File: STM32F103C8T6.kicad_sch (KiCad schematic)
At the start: 32 parts, among them J1 USB_B_Micro, J2 Conn_01x04_Pin, J3 Conn_01x04_Pin, J4 Conn_01x04_Pin, SW1 SW_SPDT, U1 STM32F103C8T6, U2 AMS1117-3.3, Y1 16MHz

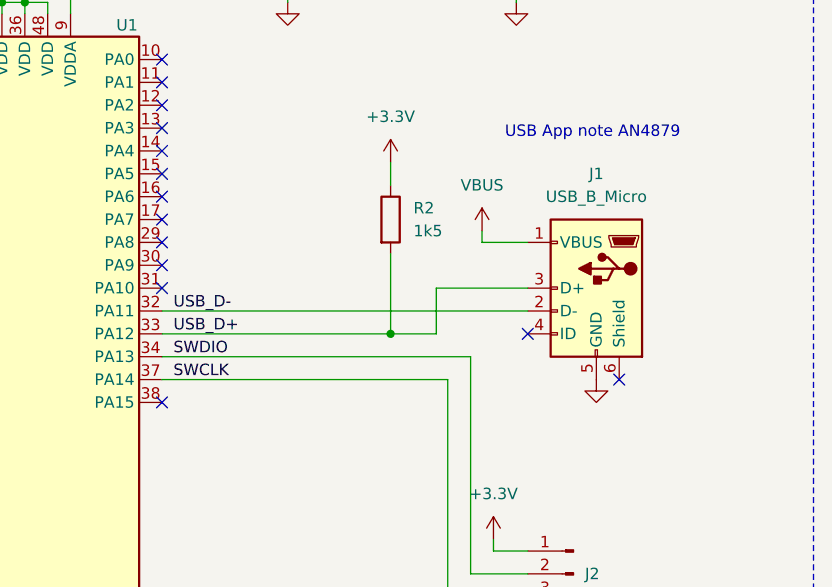
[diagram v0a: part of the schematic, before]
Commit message: updated footprints to ones which have stocks at JLCPCB
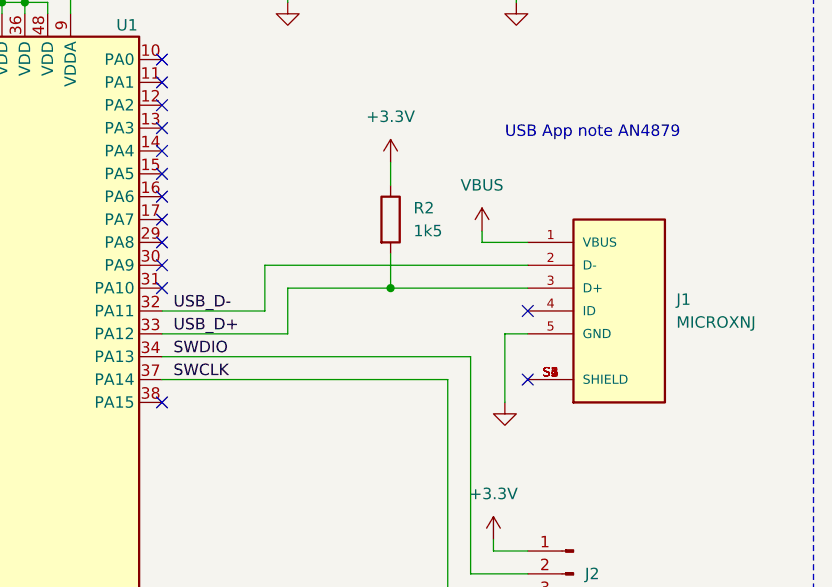
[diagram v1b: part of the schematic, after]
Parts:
- removed J1: USB_B_Micro, Connector_USB:USB_Micro-B_Wuerth_629105150521, symbol Connector:USB_B_Micro
- added J1: MICROXNJ, project_footprints:SHOUHAN_MICROXNJ, symbol MICROXNJ:MICROXNJ
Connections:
- net GND: now also J1.5 (GND)
- net USB_D+: now also J1.3 (D+)
- net USB_D-: now also J1.2 (D-)
- net VBUS: now also J1.1 (VBUS)
- new net: J1.S1 (SHIELD), J1.S2 (SHIELD), J1.S3 (SHIELD), J1.S4 (SHIELD), J1.S5 (SHIELD), J1.S6 (SHIELD)
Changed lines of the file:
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@@
   (junction (at 189.23 39.37) (diameter 0) (color 0 0 0 0)
   )
-  (junction (at 224.79 86.36) (diameter 0) (color 0 0 0 0)
-  )
   (junction (at 24.13 38.1) (diameter 0) (color 0 0 0 0)
   )
@@
   )
   (junction (at 120.65 46.99) (diameter 0) (color 0 0 0 0)
+  )
+  (junction (at 224.79 81.28) (diameter 0) (color 0 0 0 0)
   )
   (junction (at 116.84 104.14) (diameter 0) (color 0 0 0 0)
@@
   (no_connect (at 166.37 104.14))
   (no_connect (at 199.39 81.28))
+  (no_connect (at 240.03 91.44))
   (no_connect (at 166.37 114.3))
   (no_connect (at 166.37 119.38))
   (no_connect (at 199.39 60.96))
+  (no_connect (at 240.03 83.82))
   (no_connect (at 166.37 91.44))
-  (no_connect (at 240.03 86.36))
   (no_connect (at 199.39 55.88))
   (no_connect (at 199.39 68.58))
-  (no_connect (at 250.19 91.44))
   (no_connect (at 166.37 93.98))
   (no_connect (at 166.37 121.92))
@@
     (stroke (width 0) (type default))
   )
+  (wire (pts (xy 213.36 81.28) (xy 224.79 81.28))
+    (stroke (width 0) (type default))
+  )
   (wire (pts (xy 109.22 76.2) (xy 109.22 85.09))
     (stroke (width 0) (type default))
@@
     (stroke (width 0) (type default))
   )
-  (wire (pts (xy 240.03 81.28) (xy 229.87 81.28))
+  (wire (pts (xy 224.79 81.28) (xy 240.03 81.28))
     (stroke (width 0) (type default))
   )
@@
     (stroke (width 0) (type default))
   )
-  (wire (pts (xy 229.87 86.36) (xy 224.79 86.36))
+  (wire (pts (xy 237.49 86.36) (xy 240.03 86.36))
     (stroke (width 0) (type default))
   )
@@
   )
   (wire (pts (xy 116.84 104.14) (xy 109.22 104.14))
+    (stroke (width 0) (type default))
+  )
+  (wire (pts (xy 237.49 93.98) (xy 237.49 86.36))
     (stroke (width 0) (type default))
   )
@@
     (stroke (width 0) (type default))
   )
-  (wire (pts (xy 224.79 86.36) (xy 199.39 86.36))
-    (stroke (width 0) (type default))
-  )
   (wire (pts (xy 129.54 147.32) (xy 130.81 147.32))
     (stroke (width 0) (type default))
@@
     (stroke (width 0) (type default))
   )
+  (wire (pts (xy 199.39 86.36) (xy 213.36 86.36))
+    (stroke (width 0) (type default))
+  )
   (wire (pts (xy 143.51 39.37) (xy 154.94 39.37))
     (stroke (width 0) (type default))
@@
     (stroke (width 0) (type default))
   )
-  (wire (pts (xy 229.87 81.28) (xy 229.87 86.36))
+  (wire (pts (xy 213.36 86.36) (xy 213.36 81.28))
     (stroke (width 0) (type default))
   )
@@
     (stroke (width 0) (type default))
   )
-  (wire (pts (xy 224.79 77.47) (xy 224.79 86.36))
+  (wire (pts (xy 224.79 77.47) (xy 224.79 81.28))
     (stroke (width 0) (type default))
   )
@@
     (stroke (width 0) (type default))
   )
+  (wire (pts (xy 210.82 78.74) (xy 240.03 78.74))
+    (stroke (width 0) (type default))
+  )
   (wire (pts (xy 154.94 85.09) (xy 154.94 68.58))
     (stroke (width 0) (type default))
@@
     (stroke (width 0) (type default))
   )
-  (wire (pts (xy 199.39 83.82) (xy 240.03 83.82))
+  (wire (pts (xy 199.39 83.82) (xy 210.82 83.82))
     (stroke (width 0) (type default))
   )
@@
   )
   (wire (pts (xy 189.23 39.37) (xy 196.85 39.37))
+    (stroke (width 0) (type default))
+  )
+  (wire (pts (xy 210.82 83.82) (xy 210.82 78.74))
     (stroke (width 0) (type default))
   )
@@
     )
   )
-  (symbol (lib_id "power:GND") (at 247.65 91.44 0) (unit 1)
-    (in_bom yes) (on_board yes) (dnp no) (fields_autoplaced)
-    (property "Reference" "#PWR012" (at 247.65 97.79 0)
-      (effects (font (size 1.27 1.27)) hide)
-    )
-    (property "Value" "GND" (at 247.65 96.52 0)
-      (effects (font (size 1.27 1.27)) hide)
-    )
-    (property "Footprint" "" (at 247.65 91.44 0)
-      (effects (font (size 1.27 1.27)) hide)
-    )
-    (property "Datasheet" "" (at 247.65 91.44 0)
-      (effects (font (size 1.27 1.27)) hide)
-    )
-    (pin "1")
-    (instances
-      (project "STM32F103C8T6"
-        (path "/7affc536-b27a-42a4-bb95-95dd3805b677"
-          (reference "#PWR012") (unit 1)
-        )
-      )
-    )
-  )
   (symbol (lib_id "power:GND") (at 120.65 49.53 0) (unit 1)
     (in_bom yes) (on_board yes) (dnp no) (fields_autoplaced)
@@
     )
   )
+  (symbol (lib_id "power:GND") (at 237.49 93.98 0) (unit 1)
+    (in_bom yes) (on_board yes) (dnp no) (fields_autoplaced)
+    (property "Reference" "#PWR025" (at 237.49 100.33 0)
+      (effects (font (size 1.27 1.27)) hide)
+    )
+    (property "Value" "GND" (at 237.49 99.06 0)
+      (effects (font (size 1.27 1.27)) hide)
+    )
+    (property "Footprint" "" (at 237.49 93.98 0)
+      (effects (font (size 1.27 1.27)) hide)
+    )
+    (property "Datasheet" "" (at 237.49 93.98 0)
+      (effects (font (size 1.27 1.27)) hide)
+    )
+    (pin "1")
+    (instances
+      (project "STM32F103C8T6"
+        (path "/7affc536-b27a-42a4-bb95-95dd3805b677"
+          (reference "#PWR025") (unit 1)
+        )
+      )
+    )
+  )
   (symbol (lib_id "power:GND") (at 24.13 54.61 0) (unit 1)
     (in_bom yes) (on_board yes) (dnp no) (fields_autoplaced)
@@
         (path "/7affc536-b27a-42a4-bb95-95dd3805b677"
           (reference "C8") (unit 1)
-        )
-      )
-    )
-  )
-  (symbol (lib_id "Connector:USB_B_Micro") (at 247.65 81.28 0) (mirror y) (unit 1)
-    (in_bom yes) (on_board yes) (dnp no)
-    (property "Reference" "J1" (at 247.65 68.58 0)
-      (effects (font (size 1.27 1.27)))
-    )
-    (property "Value" "USB_B_Micro" (at 247.65 71.12 0)
-      (effects (font (size 1.27 1.27)))
-    )
-    (property "Footprint" "Connector_USB:USB_Micro-B_Wuerth_629105150521" (at 243.84 82.55 0)
-      (effects (font (size 1.27 1.27)) hide)
-    )
-    (property "Datasheet" "~" (at 243.84 82.55 0)
-      (effects (font (size 1.27 1.27)) hide)
-    )
-    (pin "1")
-    (pin "2")
-    (pin "3")
-    (pin "5")
-    (pin "4")
-    (pin "6")
-    (instances
-      (project "STM32F103C8T6"
-        (path "/7affc536-b27a-42a4-bb95-95dd3805b677"
-          (reference "J1") (unit 1)
         )
       )
@@
         )
       )
+    )
+  )
+  (symbol (lib_id "MICROXNJ:MICROXNJ") (at 250.19 83.82 0) (unit 1)
+    (in_bom yes) (on_board yes) (dnp no) (fields_autoplaced)
+    (property "Reference" "J1" (at 256.54 82.55 0)
+      (effects (font (size 1.27 1.27)) (justify left))
+    )
+    (property "Value" "MICROXNJ" (at 256.54 85.09 0)
+      (effects (font (size 1.27 1.27)) (justify left))
+    )
+    (property "Footprint" "project_footprints:SHOUHAN_MICROXNJ" (at 250.19 83.82 0)
+      (effects (font (size 1.27 1.27)) (justify bottom) hide)
+    )
+    (property "Datasheet" "" (at 250.19 83.82 0)
+      (effects (font (size 1.27 1.27)) hide)
+    )
+    (property "MF" "Shouhan" (at 250.19 83.82 0)
+      (effects (font (size 1.27 1.27)) (justify bottom) hide)
+    )
+    (property "MAXIMUM_PACKAGE_HEIGHT" "3mm" (at 250.19 83.82 0)
+      (effects (font (size 1.27 1.27)) (justify bottom) hide)
+    )
+    (property "Package" "Package" (at 250.19 83.82 0)
+      (effects (font (size 1.27 1.27)) (justify bottom) hide)
+    )
+    (property "Price" "None" (at 250.19 83.82 0)
+      (effects (font (size 1.27 1.27)) (justify bottom) hide)
+    )
+    (property "Check_prices" "https://www.snapeda.com/parts/MICROXNJ/Shouhan/view-part/?ref=eda" (at 250.19 83.82 0)
+      (effects (font (size 1.27 1.27)) (justify bottom) hide)
+    )
+    (property "STANDARD" "Manufacturer Recommendations" (at 250.19 83.82 0)
+      (effects (font (size 1.27 1.27)) (justify bottom) hide)
+    )
+    (property "PARTREV" "A" (at 250.19 83.82 0)
+      (effects (font (size 1.27 1.27)) (justify bottom) hide)
+    )
+    (property "SnapEDA_Link" "https://www.snapeda.com/parts/MICROXNJ/Shouhan/view-part/?ref=snap" (at 250.19 83.82 0)
+      (effects (font (size 1.27 1.27)) (justify bottom) hide)
+    )
+    (property "MP" "MICROXNJ" (at 250.19 83.82 0)
+      (effects (font (size 1.27 1.27)) (justify bottom) hide)
+    )
+    (property "Description" "\nSensor Cables / Actuator Cables\n" (at 250.19 83.82 0)
+      (effects (font (size 1.27 1.27)) (justify bottom) hide)
+    )
+    (property "Availability" "Not in stock" (at 250.19 83.82 0)
+      (effects (font (size 1.27 1.27)) (justify bottom) hide)
+    )
+    (property "MANUFACTURER" "SHOUHAN" (at 250.19 83.82 0)
+      (effects (font (size 1.27 1.27)) (justify bottom) hide)
+    )
+    (pin "S5")
+    (pin "S6")
+    (pin "4")
+    (pin "5")
+    (pin "S1")
+    (pin "S2")
+    (pin "S3")
+    (pin "S4")
+    (pin "3")
+    (pin "2")
+    (pin "1")
+    (instances
+      (project "STM32F103C8T6"
+        (path "/7affc536-b27a-42a4-bb95-95dd3805b677"
+          (reference "J1") (unit 1)
+        )
+      )

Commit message: changed footprint of the ferrite bead
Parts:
- C1: footprint Capacitor_SMD:C_0603_1608Metric -> Capacitor_SMD:C_0805_2012Metric
- FB1: footprint Inductor_SMD:L_0603_1608Metric -> Capacitor_SMD:C_0805_2012Metric
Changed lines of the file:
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@@
   (title_block
     (title "STM32F103C8T6 Basic PCB")
-    (date "2024-01-01")
-    (rev "0.1")
+    (date "2024-01-06")
+    (rev "0.2")
     (company "Matia's Lab")
   )
@@
       (effects (font (size 1.27 1.27)) (justify left))
     )
-    (property "Footprint" "Capacitor_SMD:C_0603_1608Metric" (at 121.6152 46.99 0)
+    (property "Footprint" "Capacitor_SMD:C_0805_2012Metric" (at 121.6152 46.99 0)
       (effects (font (size 1.27 1.27)) hide)
     )
@@
       (effects (font (size 1.27 1.27)))
     )
-    (property "Footprint" "Inductor_SMD:L_0603_1608Metric" (at 227.33 41.148 90)
-      (effects (font (size 1.27 1.27)) hide)
-    )
+    (property "Footprint" "Capacitor_SMD:C_0805_2012Metric" (at 227.33 41.148 90)
+      (effects (font (size 1.27 1.27)) hide)
+    )
